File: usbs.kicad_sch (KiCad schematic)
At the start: 17 parts, among them J4 USB-A_Amphenol_UE27AC54100, J5 USB-C_GCT_USB4105-GF-A, J6 USB-C_GCT_USB4105-GF-A, U4 FT234XD-R

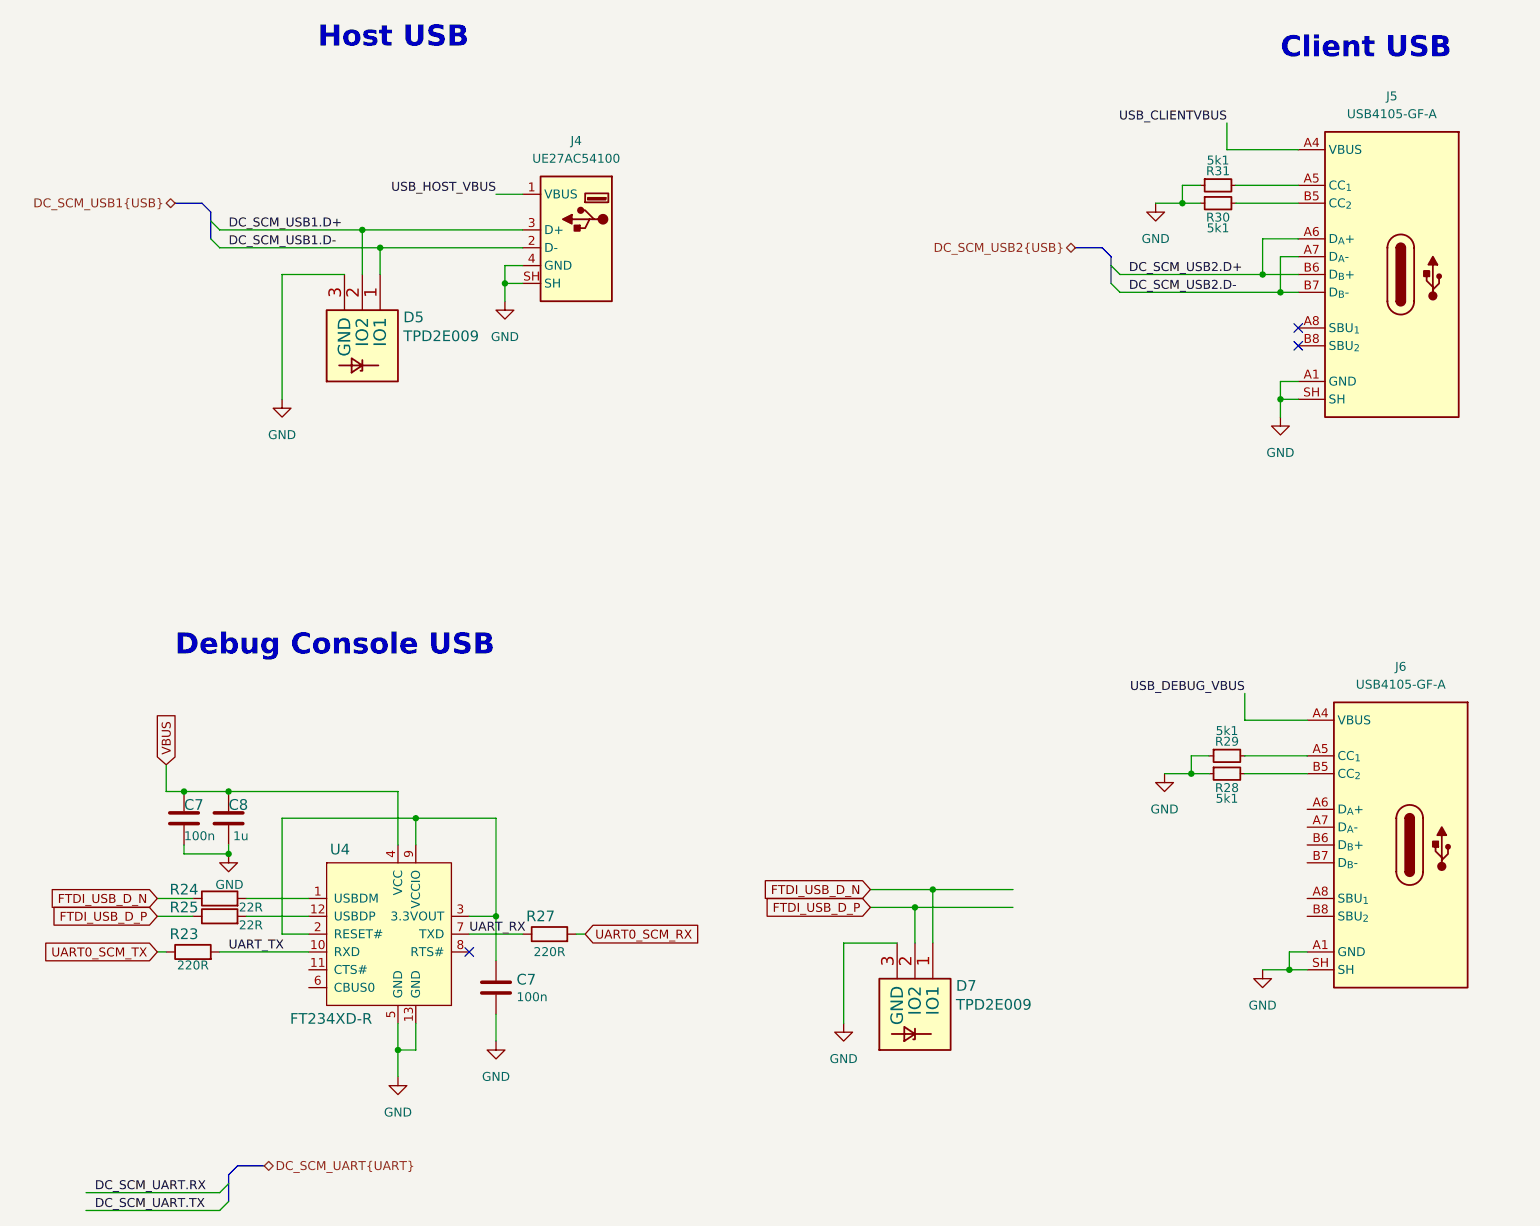
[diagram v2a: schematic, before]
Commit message: [#92504] Add Debug USB
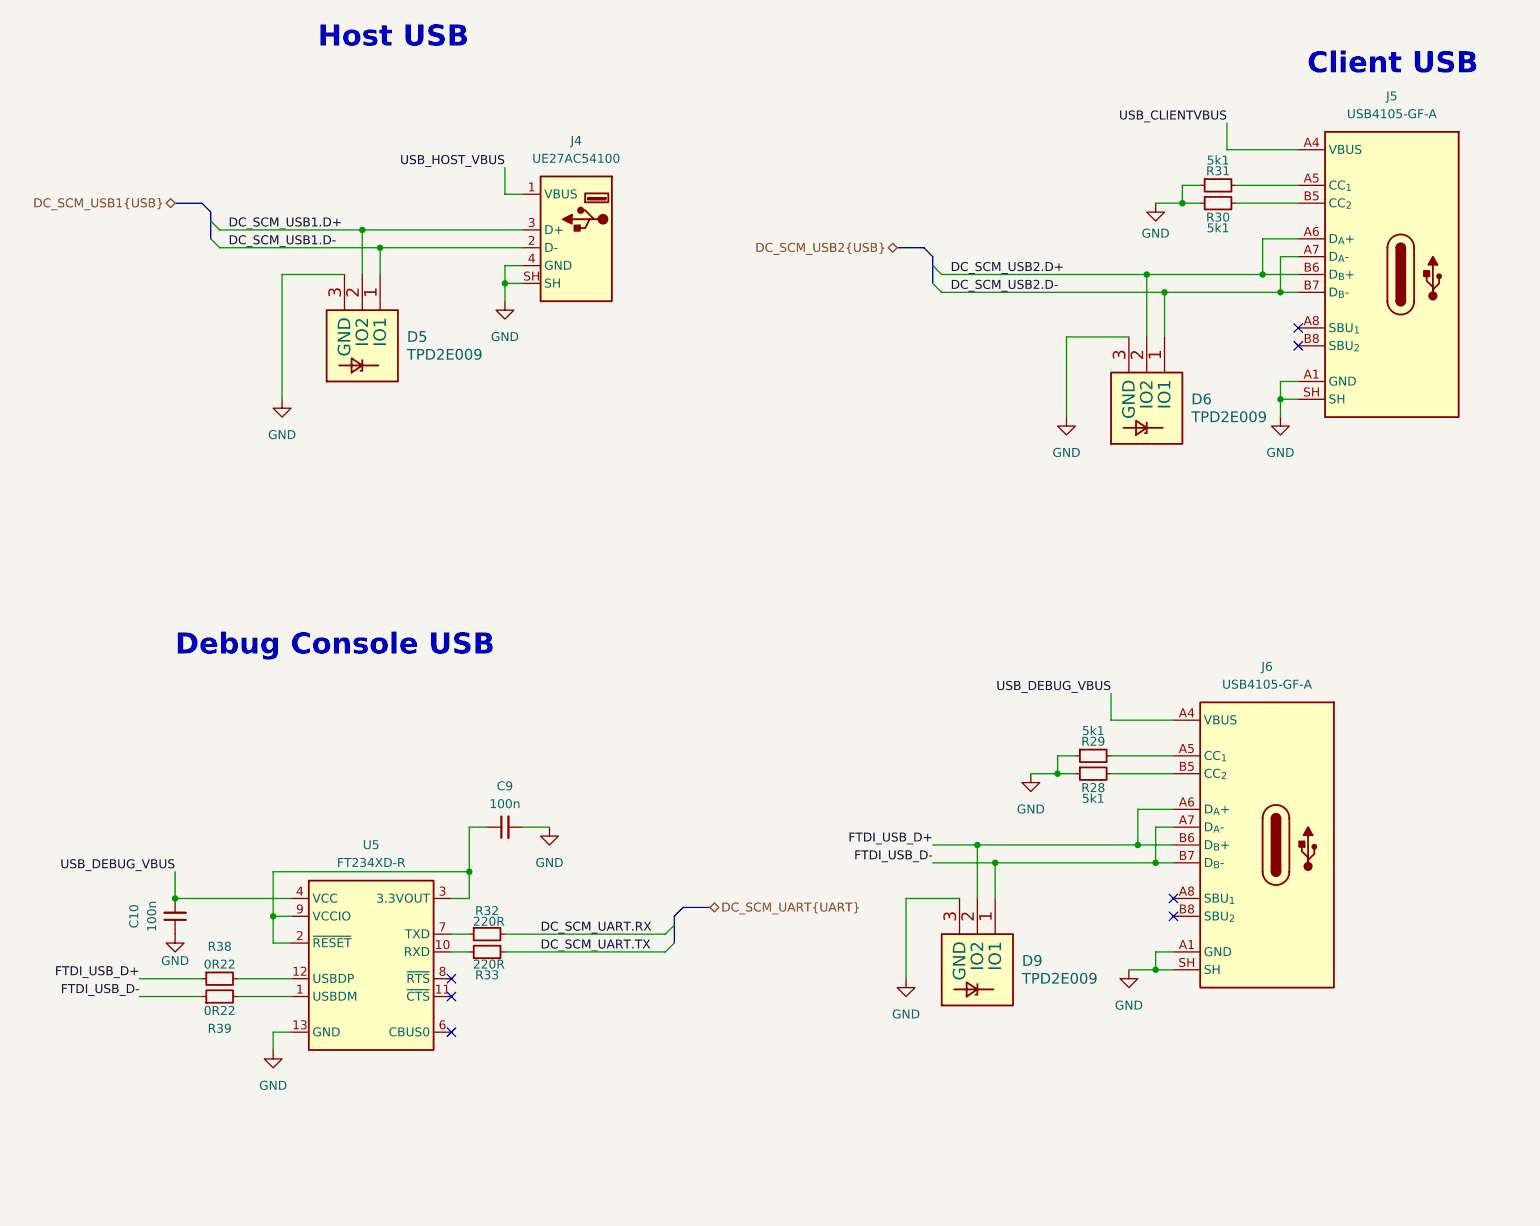
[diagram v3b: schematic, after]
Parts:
- removed C7 (x2): C_100n_0402, bmc-breakout-board-footprints:0402-cap, symbol bmc-breakout-board:C_100n_0402
- removed C8: C_1u_0402, bmc-breakout-board-footprints:0402-cap, symbol bmc-breakout-board:C_1u_0402
- removed D7: TPD2E009, bmc-breakout-board-footprints:SOT-3, symbol bmc-breakout-board:TPD2E009
- removed R23, R27: R_220R_0402, bmc-breakout-board-footprints:0402-res, symbol bmc-breakout-board:R_220R_0402
- removed R24, R25: R_22R_0402, bmc-breakout-board-footprints:0402-res, symbol bmc-breakout-board:R_22R_0402
- removed U4: FT234XD-R, bmc-breakout-board-footprints:DFN-12-1EP_3x3mm, symbol bmc-breakout-board:FT234XD-R
- added C10, C9: C_100n_16V_X7R_0402, antmicro-footprints:C_0402_1005Metric, symbol antmicroCapacitors0402:C_100n_16V_X7R_0402
- added D6, D9: TPD2E009, bmc-breakout-board-footprints:SOT-3, symbol bmc-breakout-board:TPD2E009
- added R32, R33: R_220R_0402, antmicro-footprints:R_0402_1005Metric, symbol antmicroResistors0402:R_220R_0402
- added R38, R39: R_0R22_0402, antmicro-footprints:R_0402_1005Metric, symbol antmicroResistors0402:R_0R22_0402
- added U5: FT234XD-R, antmicro-footprints:DFN-12-1EP_3x3mm, symbol antmicroInterfaceControllers:FT234XD-R
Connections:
- net DC_SCM_UART.RX: now also R32.2
- net DC_SCM_UART.TX: now also R33.2
- net DC_SCM_USB2.D+: now also D6.2 (IO2)
- net DC_SCM_USB2.D-: now also D6.1 (IO1)
- net GND: now also C10.1, C9.2, D6.3 (GND), D9.3 (GND), U5.13 (GND), U5.5 (GND)
- net USB_DEBUG_VBUS: now also C10.2, U5.4 (VCC)
- net FTDI_USB_D+: now reaches J6.A6 (D_{A}+)
- net FTDI_USB_D+: now also J6.B6 (D_{B}+), D9.2 (IO2), R38.1
- net FTDI_USB_D-: now reaches J6.A7 (D_{A}-)
- net FTDI_USB_D-: now also J6.B7 (D_{B}-), D9.1 (IO1), R39.1
- new net: R33.1, U5.10 (RXD)
- new net: C9.1, U5.2 (~{RESET}), U5.3 (3.3VOUT), U5.9 (VCCIO)
- new net: R39.2, U5.1 (USBDM)
- new net: R38.2, U5.12 (USBDP)
- new net: R32.1, U5.7 (TXD)
- no-connect marks 3 -> 7
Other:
- moved on the sheet: J6, R28, R29

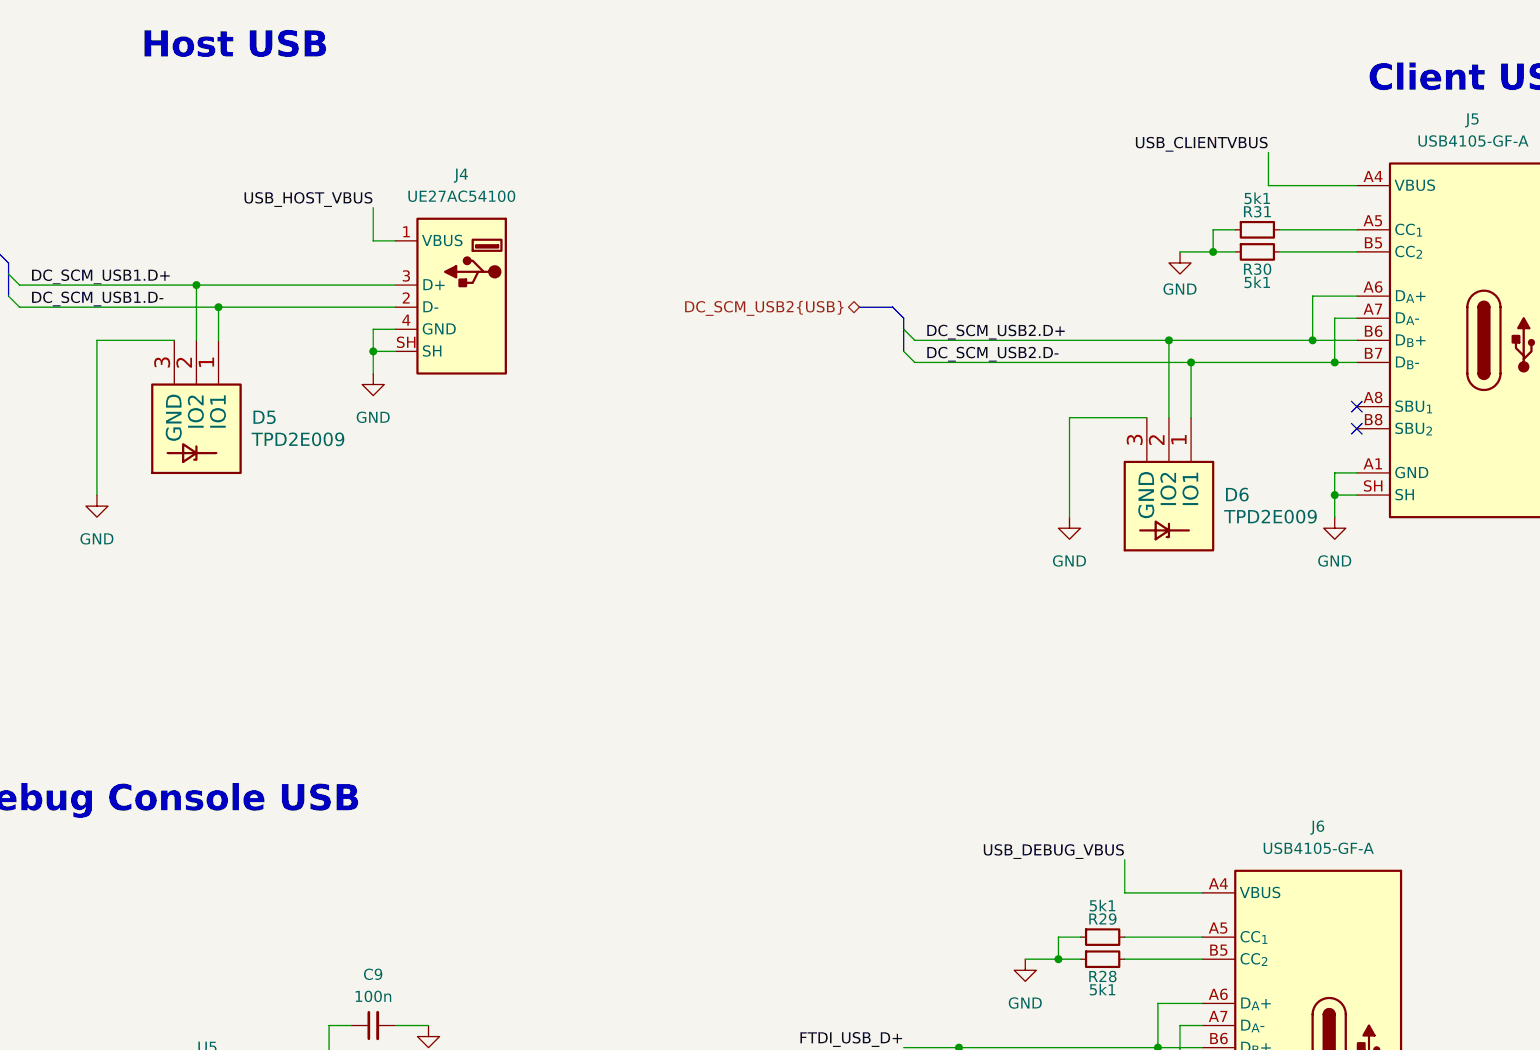
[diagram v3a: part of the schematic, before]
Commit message: [#92504] Clear ERC errors
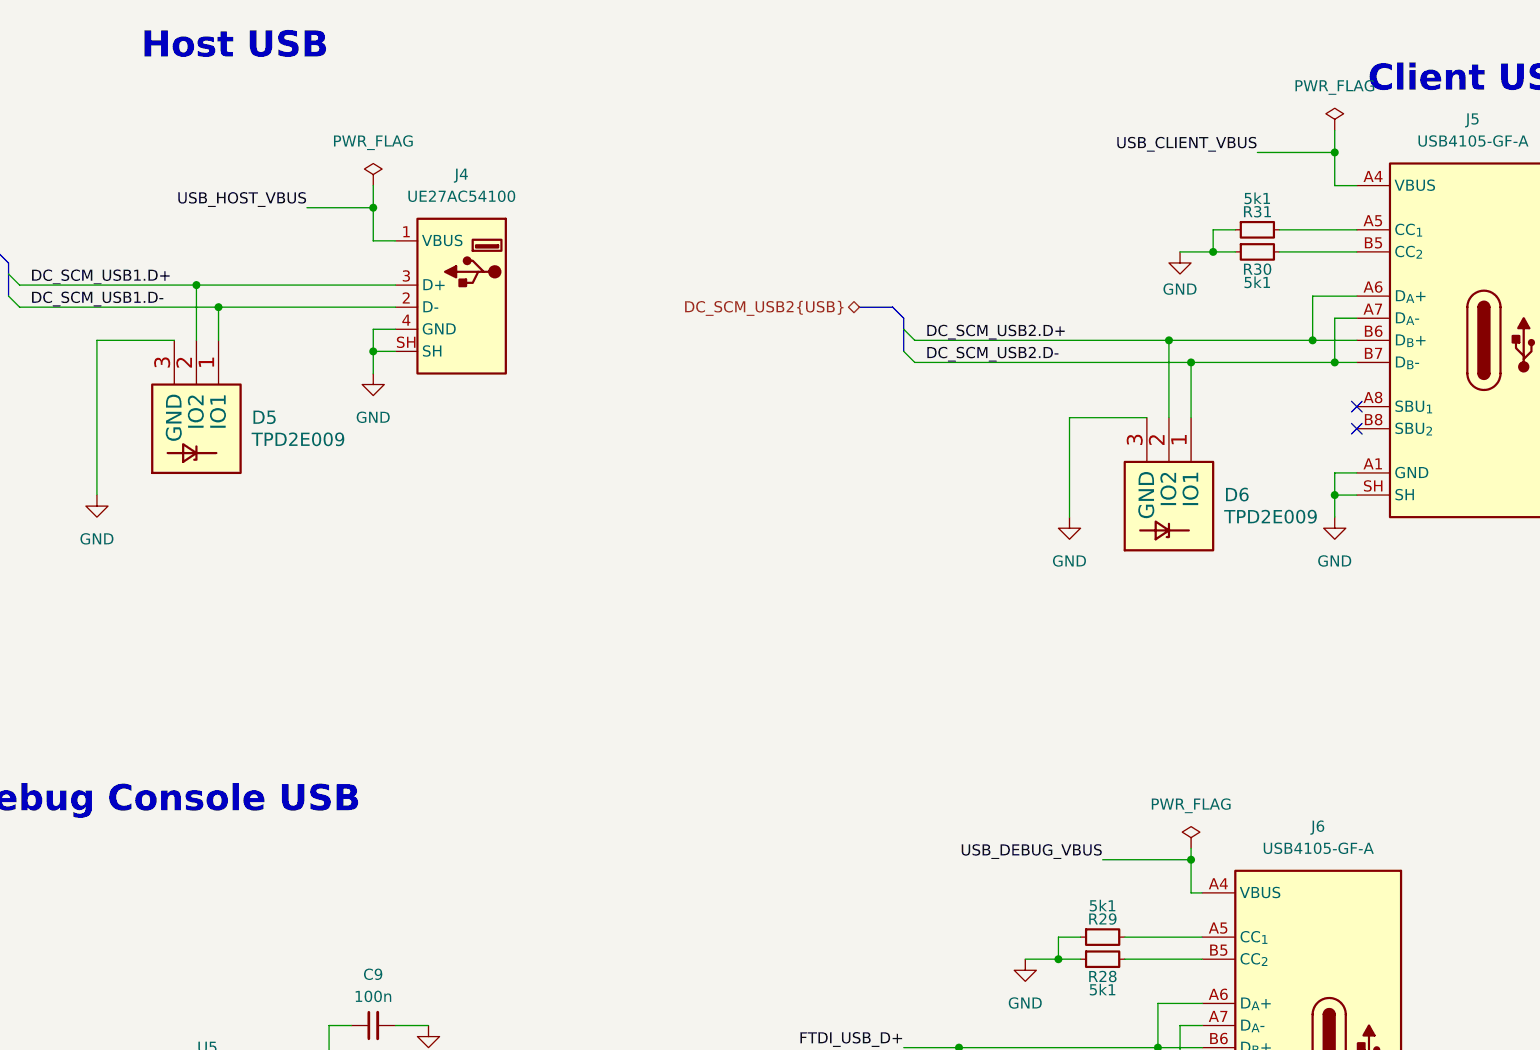
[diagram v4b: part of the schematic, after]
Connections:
- net USB_CLIENTVBUS renamed USB_CLIENT_VBUS
